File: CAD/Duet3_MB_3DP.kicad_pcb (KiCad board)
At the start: 4 copper layers, 101.9 x 125 mm, 261 parts, among them J1 SWD, J16 EXPANSION, J17 ESP_DB, J18 250-502/000-006, J19 A2543WV-5P, J2 A2543WV-2P, J27 uSD_Socket, J30 LASER/VFD, J33 A2543WV-4P, J34 A2543WV-4P, J43 USB, J46 ETHERNET, J48 SBC, J49 A2543WV-2P, J59 A2543WV-2P, J60 A2543WV-2P, M1 FID, M11 MOUNTING, M12 Logo_KICAD, M15 MOUNTING, M2 FID, M3 MOUNTING, M9 MOUNTING, Q1 BC807, Q21 MMBTA06-7-F, Q22 MMBTA06-7-F, U1 SN74F125DR, U11 ATSAME70Q20B-ANT, U13 MCP2542, U16 KSZ8081RNACA, U17 74LVC2G125, U19 74LVC2G34, U2 SN74F125DR, U20 Optoisolator, U21 SN74F125DR, U22 SN74F125DR, U23 Optoisolator, U24 LM70860RRXR, U27 Optoisolator, U28 Optoisolator, U3 EMIF06, U4 AP7361C-33E-13, U5 RClamp0504FB, U6 SN74F125DR, U7 AP22816AKEWT, U9 74HCT365, X1 ECS-120-10-33B-CKM-TR, X2 25Mhz

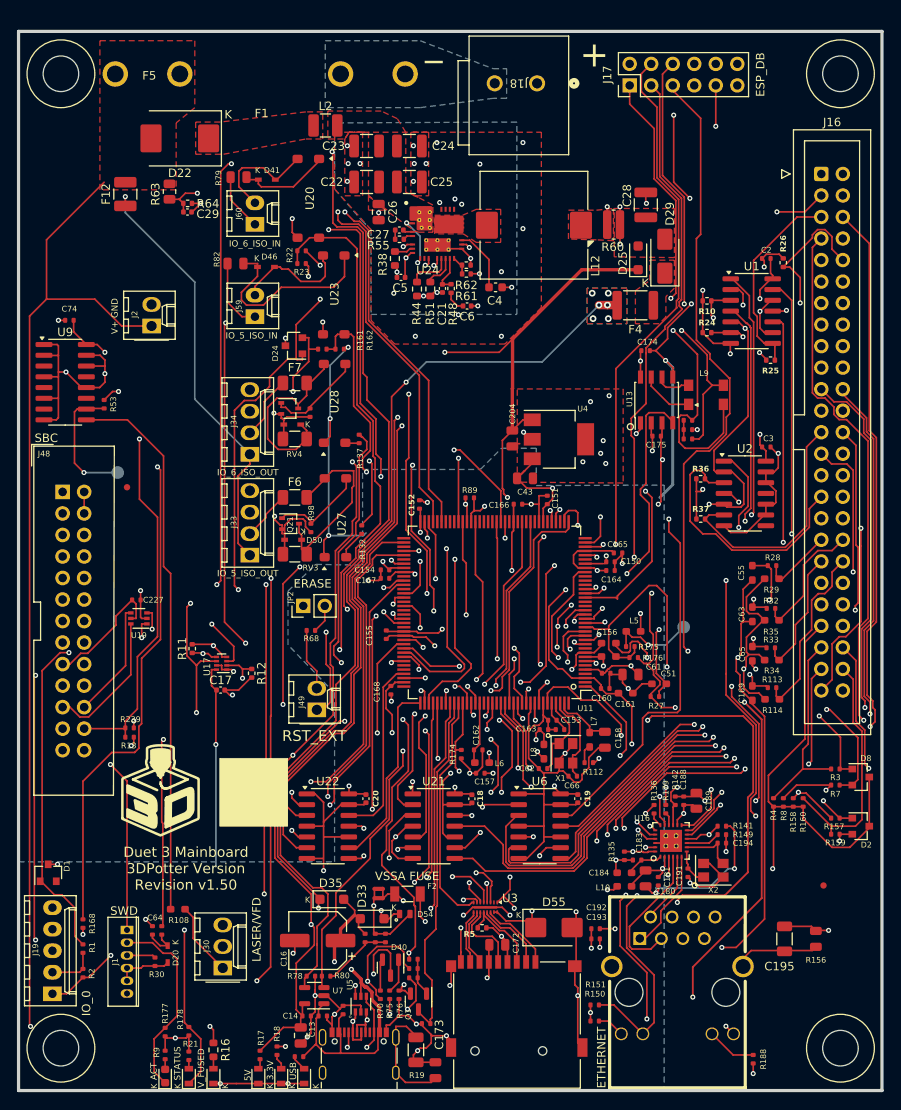
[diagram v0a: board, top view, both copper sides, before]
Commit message: QOL
Added a buttload of 3d models, 3d model of board is now usable. Also saved a lot of missing symbols and footprints, which are available in the 3DPotter Library.
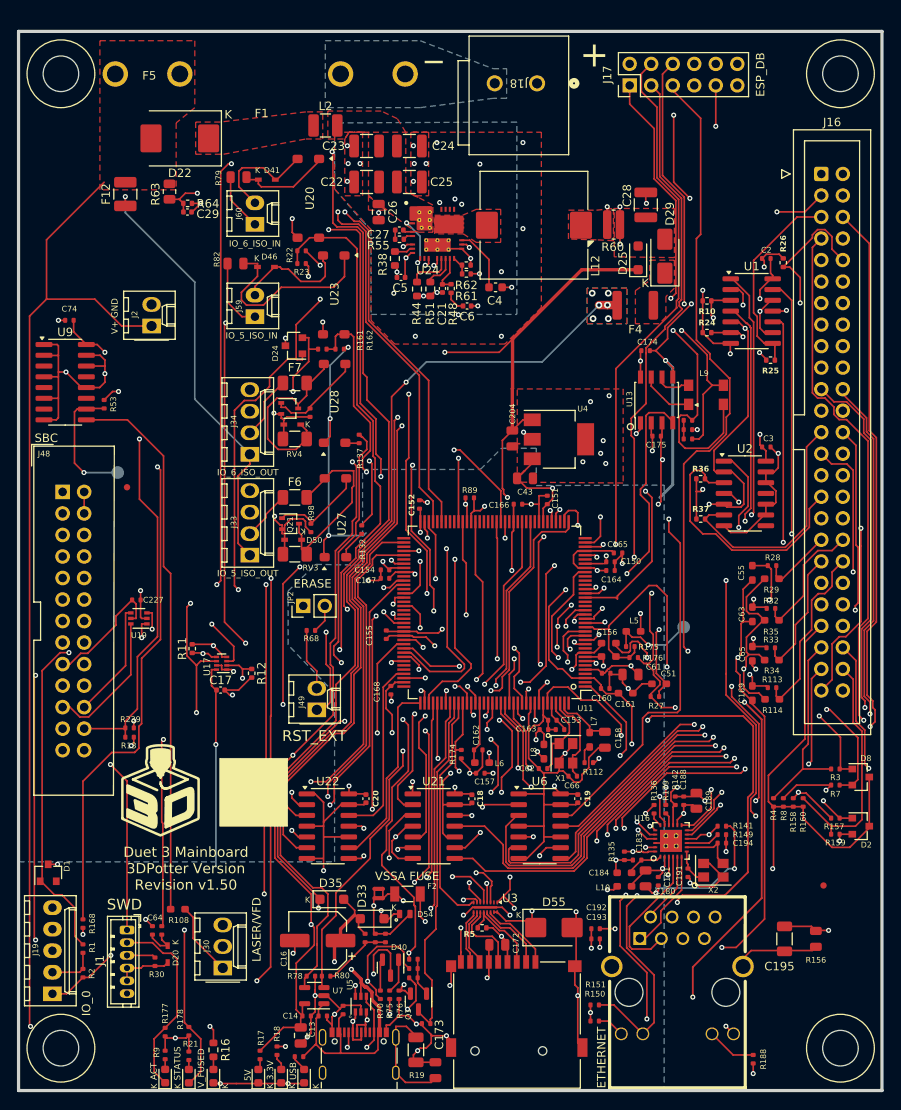
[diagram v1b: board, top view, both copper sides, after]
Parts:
- F4: footprint Fuse:Fuse_1812_4532Metric -> 3DPotter:Fuse_1812_4532Metric
- J1: footprint complib:JST_ZH_1x06_P1.5_B6B-ZR-SM4-TF -> 3DPotter:JST_ZH_B6B-ZR_1x06_P1.50mm_Vertical
- J27: footprint complib:uSD_SKT -> 3DPotter:uSD_SKT
- J43: footprint complib:USB_C_Receptacle_Valcon_CSP-USC16-TR -> 3DPotter:USB_C_Receptacle_Valcon_CSP-USC16-TR
- J46: footprint complib:RJ45+MAG -> 3DPotter:RJ45+MAG
- moved J1 3.75 mm to (71.8, 195.2), turned to -90 degrees

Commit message: 12 Unconnected left
Almost done :) Brian fried
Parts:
- removed C18, C19, C20: 100nF 16V, Capacitor_SMD:C_0402_1005Metric
- removed C2, C3: 100nF 16V, Capacitor_SMD:C_0402_1005Metric_Wbry
- removed R10, R24, R25, R26, R36, R37: 100K, Resistor_SMD:R_0402_1005Metric
- removed U1, U2, U21, U22, U6: SN74F125DR, Package_SO:SOIC-14_3.9x8.7mm_P1.27mm
- added C30: 100nF 16V, Capacitor_SMD:C_0402_1005Metric, F.Cu at (91.2, 180.0)
- added C31: 100nF 16V, Capacitor_SMD:C_0402_1005Metric, F.Cu at (100.9, 180.0)
- added C32: 100nF 16V, Capacitor_SMD:C_0402_1005Metric, F.Cu at (103.1, 179.9)
- added C33: 100nF 16V, Capacitor_SMD:C_0402_1005Metric, F.Cu at (112.6, 180.0)
- added C34: 100nF 16V, Capacitor_SMD:C_0402_1005Metric, F.Cu at (114.0, 180.0)
- added C35: 100nF 16V, Capacitor_SMD:C_0402_1005Metric, F.Cu at (123.7, 180.0)
- added R65: 47K, Resistor_SMD:R_0402_1005Metric, F.Cu at (93.6, 179.1)
- added R72: 47K, Resistor_SMD:R_0402_1005Metric, F.Cu at (105.4, 179.2)
- added R73: 47K, Resistor_SMD:R_0402_1005Metric, F.Cu at (116.1, 179.1)
- added U14: SN74LVC4245APW, 3DPotter:PW24, F.Cu at (96.3, 184.1)
- added U25: SN74LVC4245APW, 3DPotter:PW24, F.Cu at (119.0, 184.1)
- added U26: SN74LVC4245APW, 3DPotter:PW24, F.Cu at (108.0, 184.1)
- moved M1 2.77 mm to (74.5, 142.7)
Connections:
- U11 pad 57: unconnected-(U11-PD23-Pad57) -> EN_DIR_GATE
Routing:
- net D0_DIR: track 135.2 -> 0.00 mm, vias 4 -> 0
- net D_1_STEP_gated: track 20.6 -> 154.1 mm
- net D3_EN: track 114.6 -> 0.00 mm, vias 4 -> 0
- net D1_EN: track 114.2 -> 0.00 mm, vias 1 -> 0
- net D2_EN: track 111.5 -> 1.95 mm
- net D3_DIR: track 109.5 -> 0.00 mm, vias 4 -> 0
- net D2_DIR: track 107.4 -> 0.00 mm, vias 1 -> 0
- net D1_DIR: track 116.6 -> 14.8 mm
- net D5_EN: track 89.8 -> 0.00 mm, vias 1 -> 0
- net D_3_STEP_gated: track 22.1 -> 102.6 mm, vias 1 -> 4
- net EN_DIR_GATE: track 0.00 -> 76.7 mm, vias 0 -> 6
- net D4_DIR: track 73.4 -> 10.7 mm, vias 2 -> 3
- net DRIVER_0_STEP: track 88.2 -> 31.2 mm, vias 2 -> 4
- net D4_EN: track 76.1 -> 132.5 mm, vias 2 -> 3
- net D5_DIR: track 79.5 -> 134.7 mm, vias 1 -> 3
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
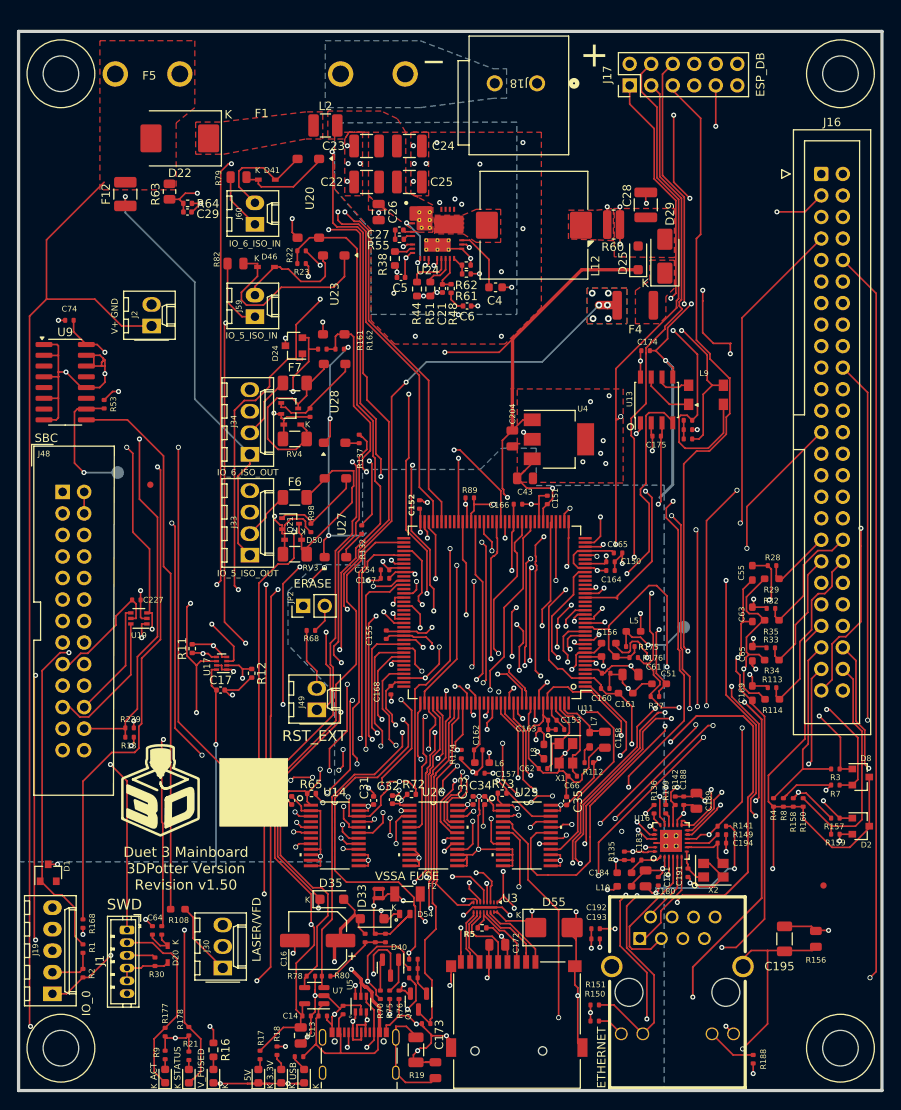
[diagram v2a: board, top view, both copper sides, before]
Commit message: 11 Unconnected
Took me while to make little progress, all because only now have I realized how bad FreeRouting's pathfinding is. So I redid a lot of the traces, bringing them all along a single path clockwise around the MCU.
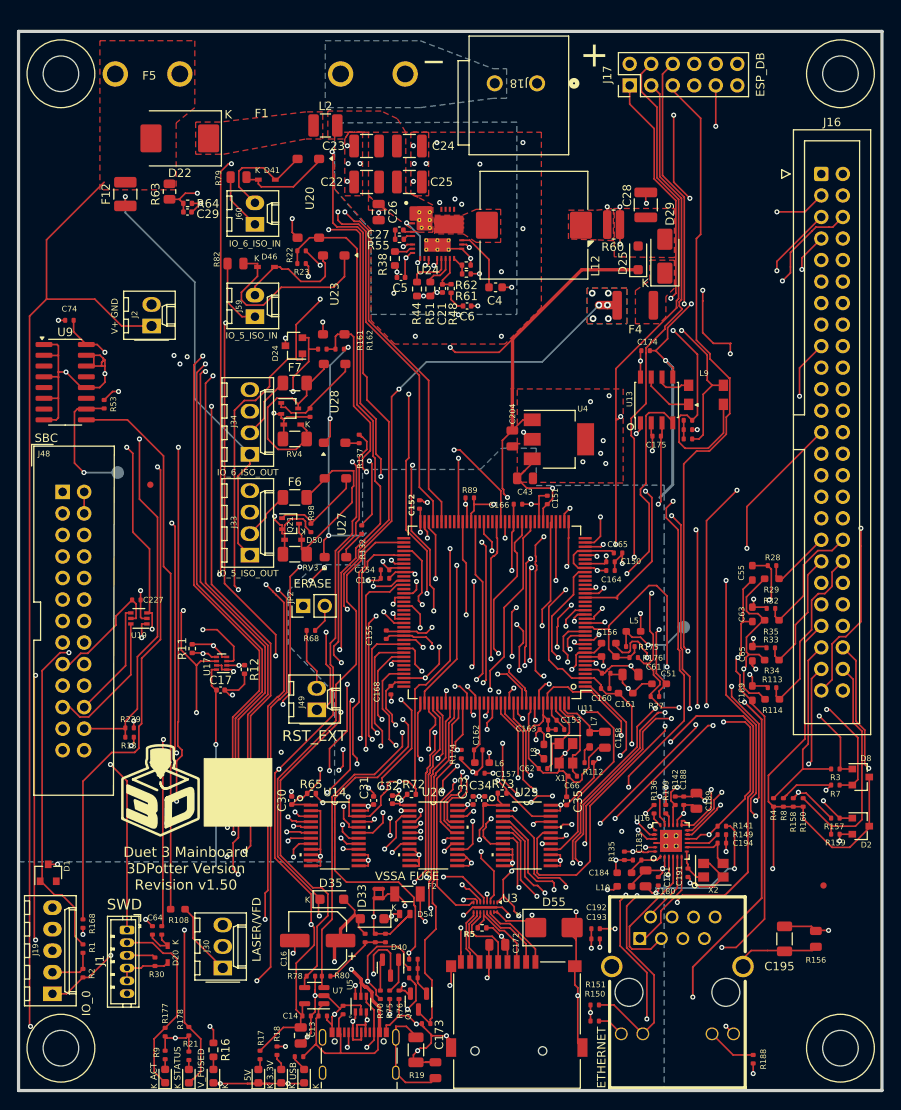
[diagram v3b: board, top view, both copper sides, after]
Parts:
- moved R12 0.96 mm to (85.7, 164.5)
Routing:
- net D1_EN: track 0.00 -> 180.0 mm, vias 0 -> 3
- net D3_EN: track 0.00 -> 167.6 mm, vias 0 -> 3
- net D1_DIR: track 14.8 -> 181.1 mm, vias 1 -> 3
- net D3_DIR: track 0.00 -> 162.5 mm, vias 0 -> 3
- net D_0_STEP_gated: track 1.92 -> 148.7 mm, vias 1 -> 3
- net D4_DIR: track 10.7 -> 152.8 mm
- net D0_DIR: track 0.00 -> 131.4 mm, vias 0 -> 3
- net D_1_STEP_gated: track 154.1 -> 59.4 mm, vias 2 -> 1
- net D_2_STEP_gated: track 0.00 -> 56.8 mm, vias 0 -> 1
- net D_4_STEP_gated: track 17.3 -> 68.6 mm, vias 1 -> 2
- net D_3_STEP_gated: track 102.6 -> 53.9 mm, vias 4 -> 1
- net D0_EN: track 151.8 -> 111.8 mm
- net D2_DIR: track 0.00 -> 29.8 mm, vias 0 -> 2
- net D2_EN: track 1.95 -> 26.0 mm, vias 1 -> 2
- net GND: track 379.2 -> 363.4 mm, vias 95 -> 98
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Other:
- board text added: "Bring everything over here, nice open space to route"

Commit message: 6 Unconnected
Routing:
- net D_1_STEP_gated: track 59.4 -> 214.1 mm, vias 1 -> 3
- net D_4_STEP_gated: track 68.6 -> 197.9 mm, vias 2 -> 3
- net D_3_STEP_gated: track 53.9 -> 132.1 mm, vias 1 -> 2
- net D_2_STEP_gated: track 56.8 -> 133.8 mm, vias 1 -> 2
- net D5_EN: track 9.63 -> 85.2 mm
- net D_0_STEP_gated: track 148.7 -> 220.0 mm, vias 3 -> 4
- net D0_EN: track 111.8 -> 182.5 mm, vias 4 -> 6
- net D2_EN: track 26.0 -> 94.3 mm
- net D2_DIR: track 29.8 -> 96.5 mm
- net D0_DIR: track 131.4 -> 197.9 mm, vias 3 -> 4
- net D5_DIR: track 136.3 -> 96.2 mm, vias 3 -> 2
- net D4_DIR: track 152.8 -> 133.3 mm
- net SWCLK: track 117.9 -> 101.6 mm, vias 3 -> 2
- net D4_EN: track 138.1 -> 125.8 mm
- net GND: track 363.4 -> 354.6 mm, vias 98 -> 96
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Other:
- board text removed: "Bring everything over here, nice open space to route"
